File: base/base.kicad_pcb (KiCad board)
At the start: 2 copper layers, 76.2 x 50.8 mm, 15 parts, among them J1 USB_B_Micro, J2 Conn_01x06, SW1 SW_Push_Open, SW2 SW_Push_Open, U1 ESP32-WROOM-32, U2 LM317_SOT-223

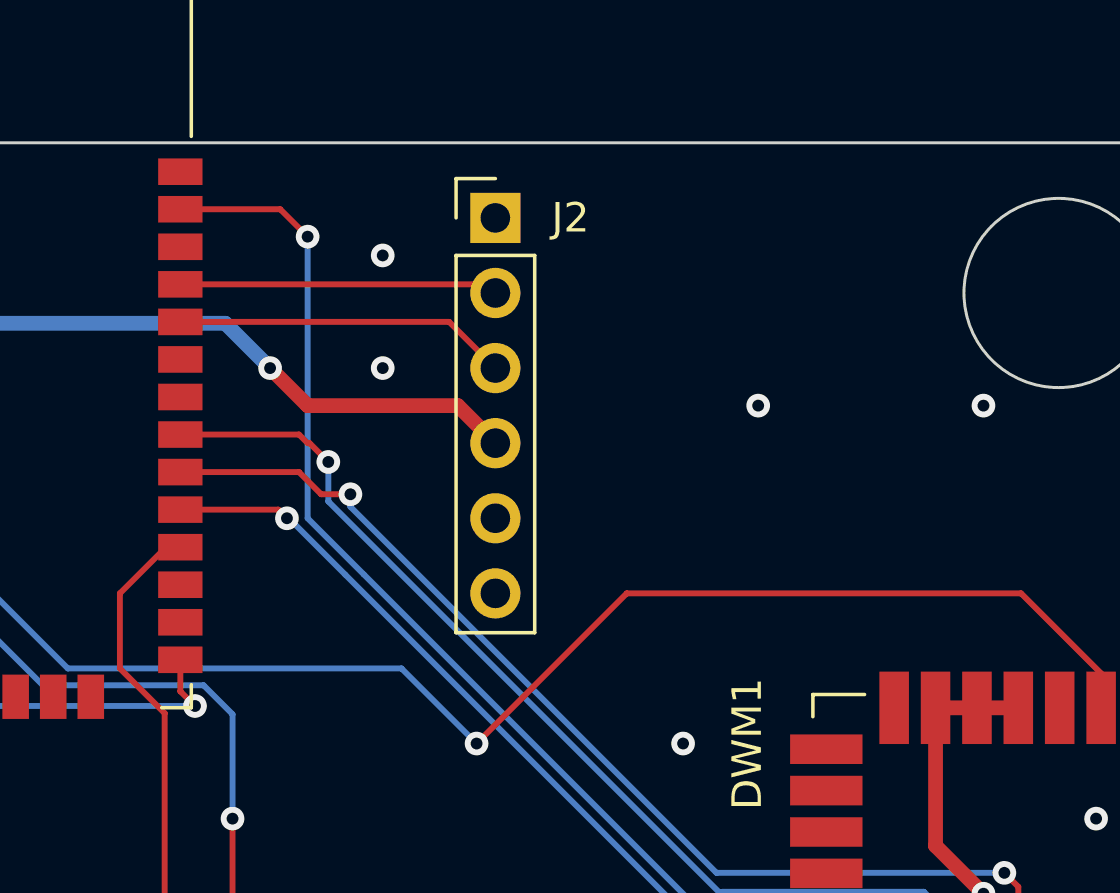
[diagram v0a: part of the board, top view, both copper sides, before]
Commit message: add BMP280 for altimeter sensor
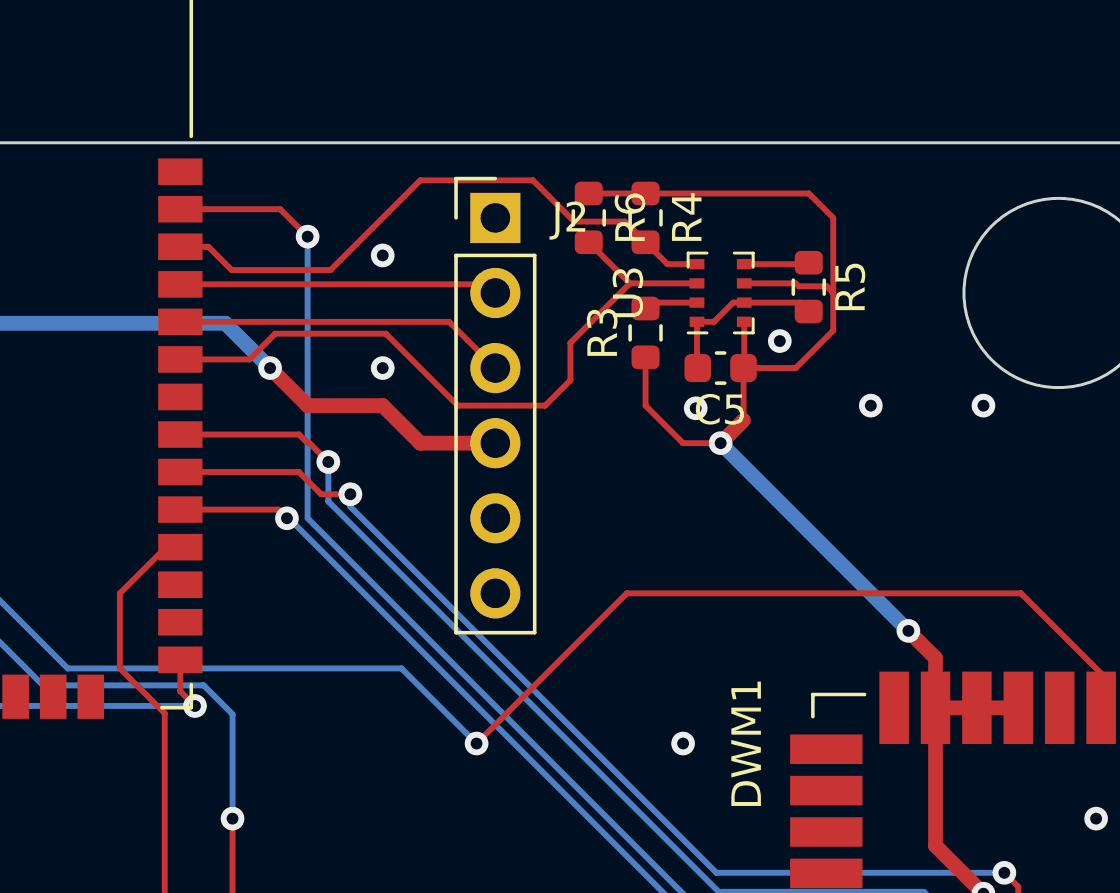
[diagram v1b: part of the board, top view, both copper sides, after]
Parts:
- added C5: C, Capacitor_SMD:C_0603_1608Metric, F.Cu at (148.6, 71.1)
- added R3: 10K, Resistor_SMD:R_0603_1608Metric, F.Cu at (146.1, 69.9)
- added R4: 10K, Resistor_SMD:R_0603_1608Metric, F.Cu at (146.1, 66.0)
- added R5: 10K, Resistor_SMD:R_0603_1608Metric, F.Cu at (151.6, 68.4)
- added R6: 10K, Resistor_SMD:R_0603_1608Metric, F.Cu at (144.1, 66.0)
- added U3: BMP280, Package_LGA:Bosch_LGA-8_2x2.5mm_P0.65mm_ClockwisePinNumbering, F.Cu at (148.6, 68.6)
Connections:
- U1 pad 33: unconnected-(U1-Pad33) -> SDA
- U1 pad 36: unconnected-(U1-Pad36) -> SCL
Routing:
- net VCC: track 140.0 -> 180.2 mm, vias 2 -> 4
- net SDA: track 0.00 -> 23.3 mm
- net SCL: track 0.00 -> 20.2 mm
- net GND: track 0.00 -> 5.75 mm, vias 18 -> 20
- net Net-(R5-Pad1): track 0.00 -> 2.20 mm
- net Net-(R3-Pad2): track 0.00 -> 1.82 mm

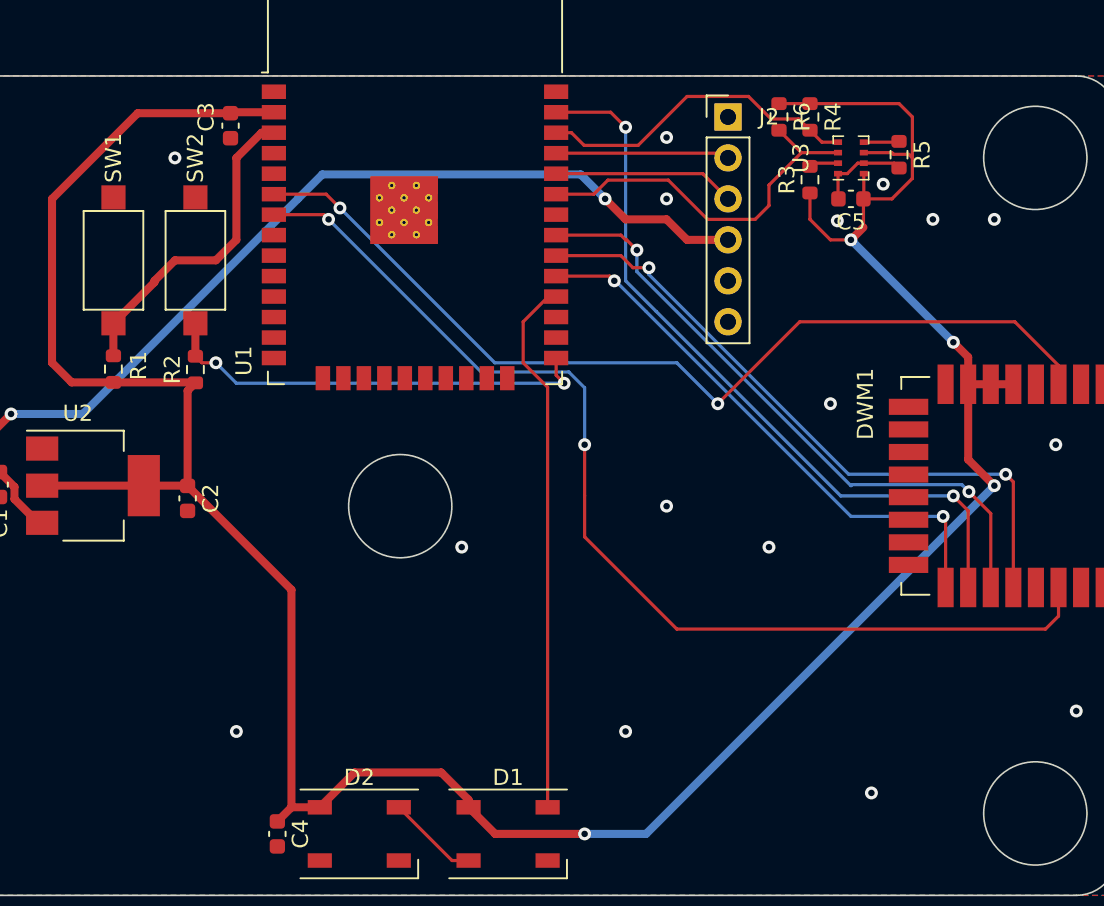
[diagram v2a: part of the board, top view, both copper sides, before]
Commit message: change rst dw1000 pin
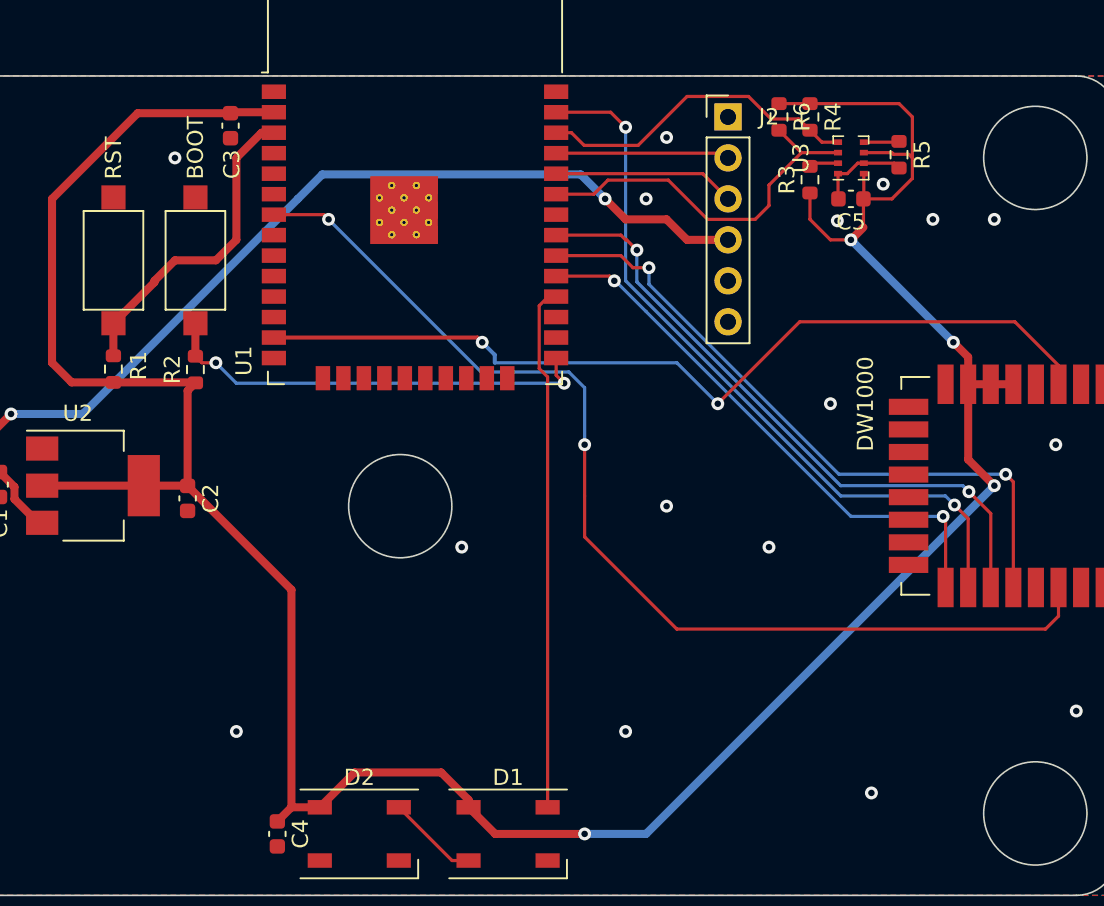
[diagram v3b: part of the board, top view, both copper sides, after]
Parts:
- renumbered SW2 to BOOT, DWM1 to DW1000, SW1 to RST
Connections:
- U1 pad 13: unconnected-(U1-Pad13) -> DW_RST
- U1 pad 6: DW_RST -> unconnected-(U1-Pad6)
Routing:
- net DW_RST: track 58.4 -> 55.0 mm
- net WS_IN: track 33.4 -> 32.6 mm

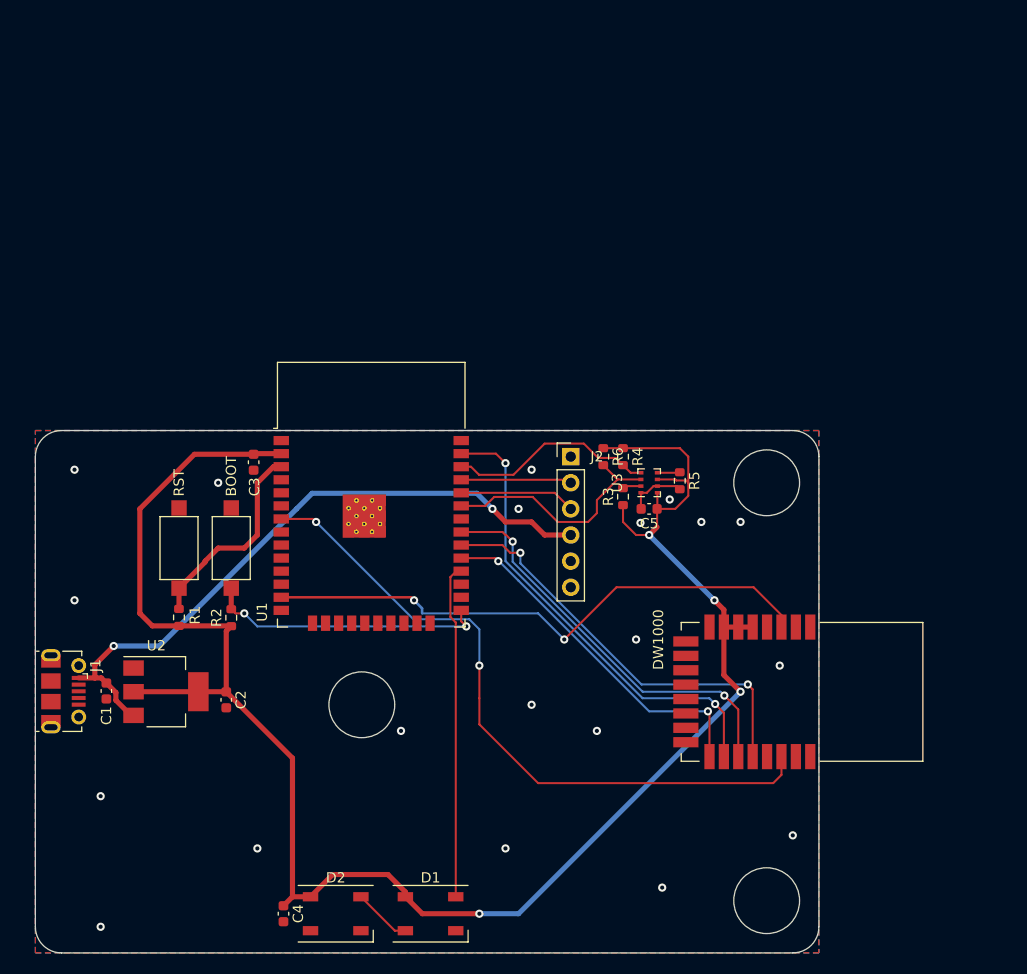
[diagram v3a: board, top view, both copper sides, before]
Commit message: add mcp73831 on base
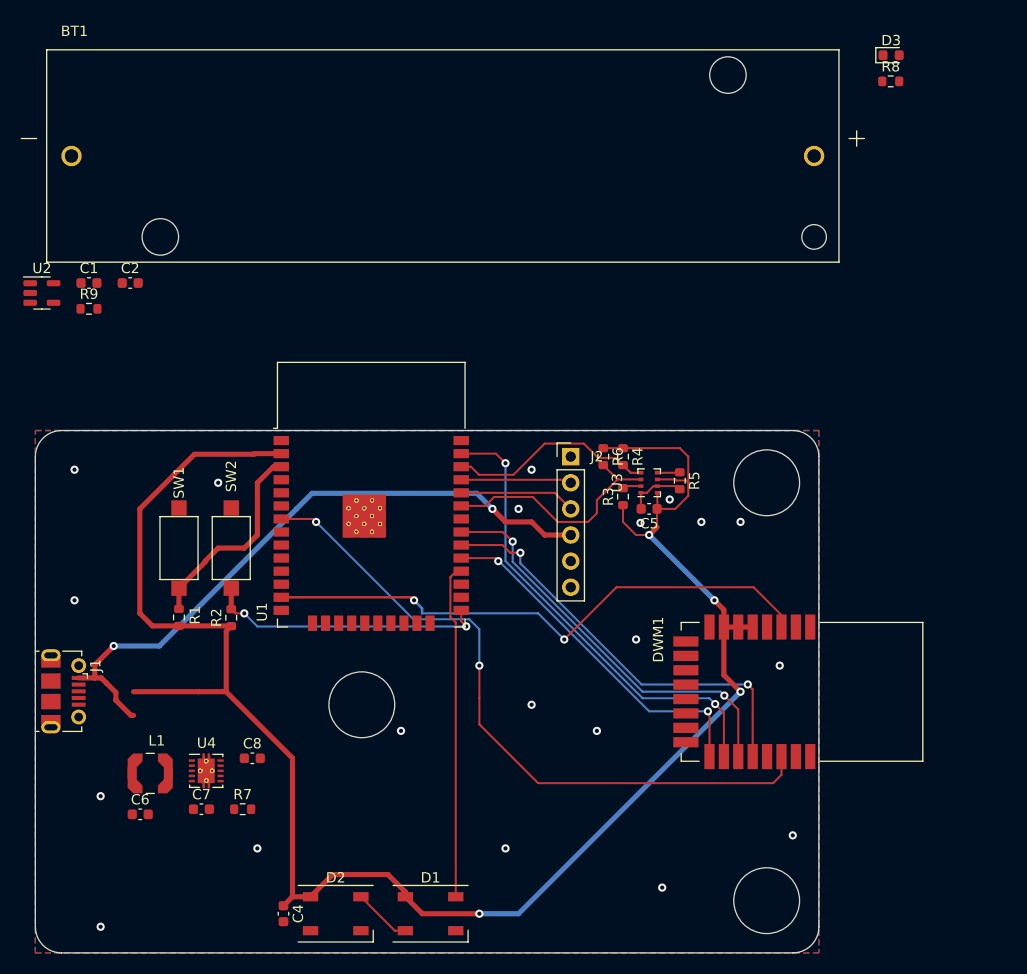
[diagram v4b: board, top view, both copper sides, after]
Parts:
- removed C3: C, Capacitor_SMD:C_0603_1608Metric
- added BT1: 1043, 18650:BAT_1043, F.Cu at (128.5, 36.8)
- added C6: 0.1uF, Capacitor_SMD:C_0603_1608Metric, F.Cu at (99.1, 100.8)
- added C7: 0.1uF, Capacitor_SMD:C_0603_1608Metric, F.Cu at (105.0, 100.3)
- added C8: 0.1uF, Capacitor_SMD:C_0603_1608Metric, F.Cu at (110.0, 95.4)
- added D3: LED, LED_SMD:LED_0603_1608Metric, F.Cu at (172.1, 27.0)
- added L1: LPS4012-103MRB, LPS4012:IND_LPS4012-103MRB, F.Cu at (100.1, 96.8)
- added R7: 100, Resistor_SMD:R_0603_1608Metric, F.Cu at (109.1, 100.3)
- added R8: 100, Resistor_SMD:R_0603_1608Metric, F.Cu at (172.1, 29.5)
- added R9: 100, Resistor_SMD:R_0603_1608Metric, F.Cu at (94.1, 51.7)
- added U4: TPS63001, Package_SON:Texas_DRC0010J_ThermalVias, F.Cu at (105.5, 96.6)
- C1, C2: value C -> 0.1uF
- U2: value LM317_SOT-223 -> MCP73831-3-OT; footprint Package_TO_SOT_SMD:SOT-223-3_TabPin2 -> Package_TO_SOT_SMD:SOT-23-5
- moved C2 41.6 mm to (98.1, 49.2), turned to 0 degrees
- moved U2 40.6 mm to (89.5, 50.1)
- moved C1 39.7 mm to (94.1, 49.2), turned to 0 degrees
- renumbered DW1000 to DWM1, RST to SW1, BOOT to SW2
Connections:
- C2 pad 1: VCC -> BAT+
- U2 pad 1: GND -> Net-(R9-Pad2)
- U2 pad 2: VCC -> GND
- U2 pad 3: 5V -> BAT+

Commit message: add battery system with charge
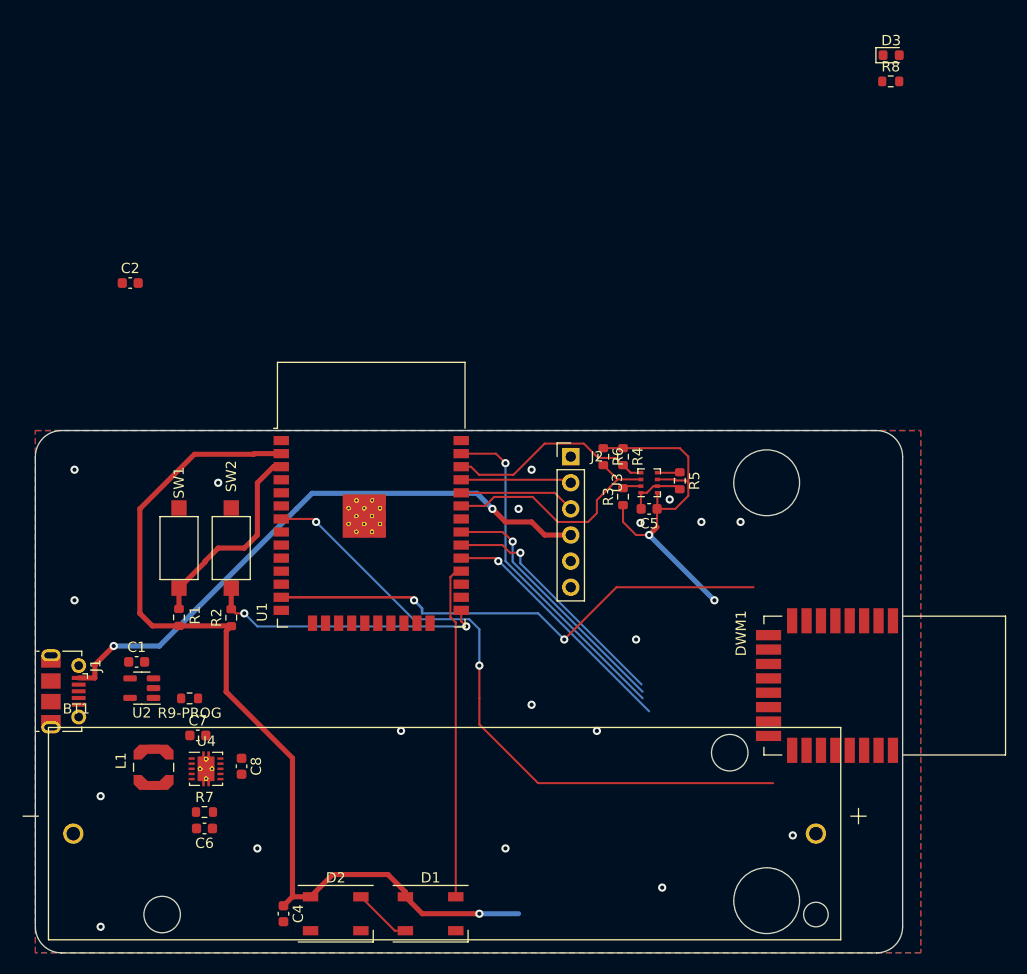
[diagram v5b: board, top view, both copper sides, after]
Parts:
- moved BT1 65.9 mm to (128.7, 102.7)
- moved U2 39.6 mm to (99.2, 88.5), turned to 180 degrees
- moved R9-PROG 39.1 mm to (103.9, 89.5), turned to 180 degrees
- moved C1 37.1 mm to (98.8, 86.0)
- moved DWM1 8.06 mm to (171.5, 88.3)
- moved C7 7.18 mm to (104.7, 93.2)
- moved C6 6.40 mm to (105.3, 102.2), turned to 180 degrees
- moved R7 3.72 mm to (105.3, 100.6)
- moved C8 1.31 mm to (109.0, 96.2), turned to -90 degrees
- moved L1 0.68 mm to (100.4, 96.2), turned to 90 degrees
- moved U4 0.20 mm to (105.5, 96.4)
- renumbered R9 to R9-PROG
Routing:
- net VCC: track 180.2 -> 128.0 mm, vias 4 -> 3
- net CLK: track 41.3 -> 23.7 mm, vias 2 -> 1
- net MISO: track 39.8 -> 25.2 mm, vias 2 -> 1
- net MOSI: track 45.8 -> 33.1 mm, vias 2 -> 1
- net SS: track 34.6 -> 24.4 mm, vias 2 -> 1
- net 5V: track 63.4 -> 57.7 mm
- net DW_RST: track 55.0 -> 50.0 mm
- net DW_IRQ: track 66.8 -> 63.9 mm
- net GND: vias 20 -> 19
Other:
- board size 76.2 x 50.8 mm -> 84.3 x 50.8 mm

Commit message: base with battery
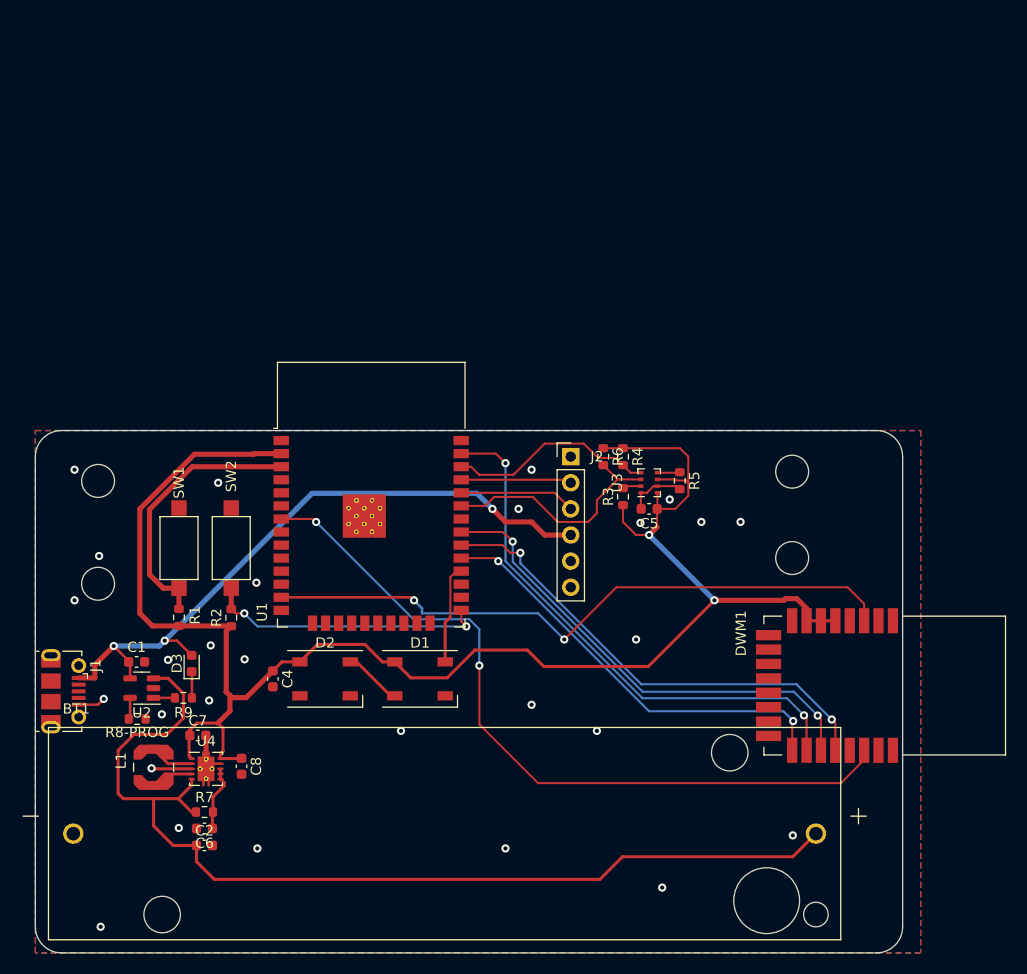
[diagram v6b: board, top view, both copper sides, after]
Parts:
- moved R8-PROG 96.0 mm to (98.8, 91.5)
- moved D3 90.1 mm to (104.1, 86.2), turned to 90 degrees
- moved C2 55.2 mm to (105.3, 103.8)
- moved C4 22.9 mm to (112.0, 87.7)
- moved D2 22.9 mm to (117.1, 87.7)
- moved D1 22.9 mm to (126.3, 87.7)
- moved R9 0.60 mm to (103.3, 89.5)
- renumbered R8 to R8-PROG, R9-PROG to R9
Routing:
- net BAT+: track 0.00 -> 100.5 mm
- net VCC: track 128.0 -> 163.4 mm, vias 3 -> 2
- net CLK: track 23.7 -> 46.8 mm, vias 1 -> 2
- net WS_IN: track 32.6 -> 9.75 mm
- net MISO: track 25.2 -> 46.7 mm, vias 1 -> 2
- net MOSI: track 33.1 -> 53.0 mm, vias 1 -> 2
- net SS: track 24.4 -> 41.7 mm, vias 1 -> 2
- net DW_RST: track 50.0 -> 63.1 mm
- net DW_IRQ: track 63.9 -> 74.6 mm
- net GND: track 5.75 -> 16.3 mm, vias 19 -> 28
- net 5V: track 57.7 -> 64.7 mm, vias 2 -> 3
- net Net-(R1-Pad2): track 19.9 -> 26.3 mm
- net Net-(C6-Pad1): track 0.00 -> 6.41 mm
- net Net-(L1-Pad2): track 0.00 -> 4.29 mm
- net Net-(L1-Pad1): track 0.00 -> 4.16 mm
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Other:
- outline, holes or cut-outs redrawn
